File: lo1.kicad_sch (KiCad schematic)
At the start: 1 part

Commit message: lo1 schematic
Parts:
- added C1, C10, C11, C15, C2, C6: 100nF, ar_passives:C_0402, symbol #bt-db:capacitor/CAPC-00573
- added C12, C13, C14, C7: 1uF, ar_passives:C_0402, symbol #bt-db:capacitor/CAPC-00622
- added C16, C17, C18, C19: 22pF, ar_passives:C_0201, symbol #bt-db:capacitor/CAPC-00021
- added C3, C4, C8: 10uF, ar_passives:C_0402, symbol #bt-db:capacitor/CAPC-00667
- added C5: 470nF, ar_passives:C_0402, symbol #bt-db:capacitor/CAPC-00613
- added C9: 10nF, ar_passives:C_0402, symbol #bt-db:capacitor/CAPC-00514
- added CLF1: 0pF, ar_passives:C_0603, symbol #bt-db:capacitor/CAPC-00674
- added CLF2, CLF3: 0pF, ar_passives:C_0402, symbol #bt-db:capacitor/CAPC-00415
- added RLF2, RLF3: TBD, ar_passives:R_0402, symbol #bt-db:resistor/RESI-00693
- U3: footprint ar_discrete:QFN40 -> ar_ic:QFN40
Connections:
- net GND: now also C10.2, C11.2, C12.2, C13.2, C14.2, C15.2, C3.2, C4.2, C5.1, C6.2, C7.2, C8.2, C9.2, CLF1.2, CLF2.2, CLF3.1
- net SYN_CE: now reaches U3.1 (CE)
- net at U3.10 (VregIN): now also C7.1
- net LO1_3V3_SYN: now reaches U3.11 (VccCP)
- net LO1_3V3_SYN: now also U3.15 (VccMASH), U3.26 (VccVCO2), U3.37 (VccVCO), U3.7 (VccDIG), C10.1, C11.1, C12.1, C13.1, C14.1
- net at U3.12 (CPout): now also CLF1.1, RLF2.1, RLF3.2
- net SYN_SCK: now reaches U3.16 (SCK)
- net SYN_SDI: now reaches U3.17 (SDI)
- net at U3.18 (RFoutBM): now also C19.1
- net at U3.19 (RFoutBP): now also C18.1
- net SYN_MUX: now reaches U3.20 (MUXout)
- net LO1_3V3_BUF: now reaches U3.21 (VccBUF)
- net LO1_3V3_BUF: now also C15.1
- net at U3.22 (RFoutAM): now also C17.1
- net at U3.23 (RFoutAP): now also C16.1
- net SYN_~{CS}: now reaches U3.24 (~{CS})
- net at U3.27 (VbiasVCO2): now also C6.1
- net at U3.29 (VrefVCO2): now also C8.1
- net at U3.3 (VbiasVCO): now also C5.2
- net SYN_RC: now reaches U3.30 (RampClk)
- net SYN_RD: now reaches U3.32 (RampDir)
- net at U3.33 (VbiasVARAC): now also C4.1
- net at U3.35 (Vtune): now also CLF3.2, RLF3.1
- net at U3.36 (VrefVCO): now also C3.1
- net at U3.38 (VregVCO): now also C9.1
- net OSC_P: now reaches U3.8 (OSCinP)
- net OSC_P: now also C1.2
- net OSC_N: now reaches U3.9 (OSCinM)
- net OSC_N: now also C2.2
- new net: CLF2.1, RLF2.2
- new net REF_N: C2.1
- new net REF_P: C1.1
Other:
- note added: "11"
- note added: "15"
- note added: "26"
- note added: "37"
- note added: "7"

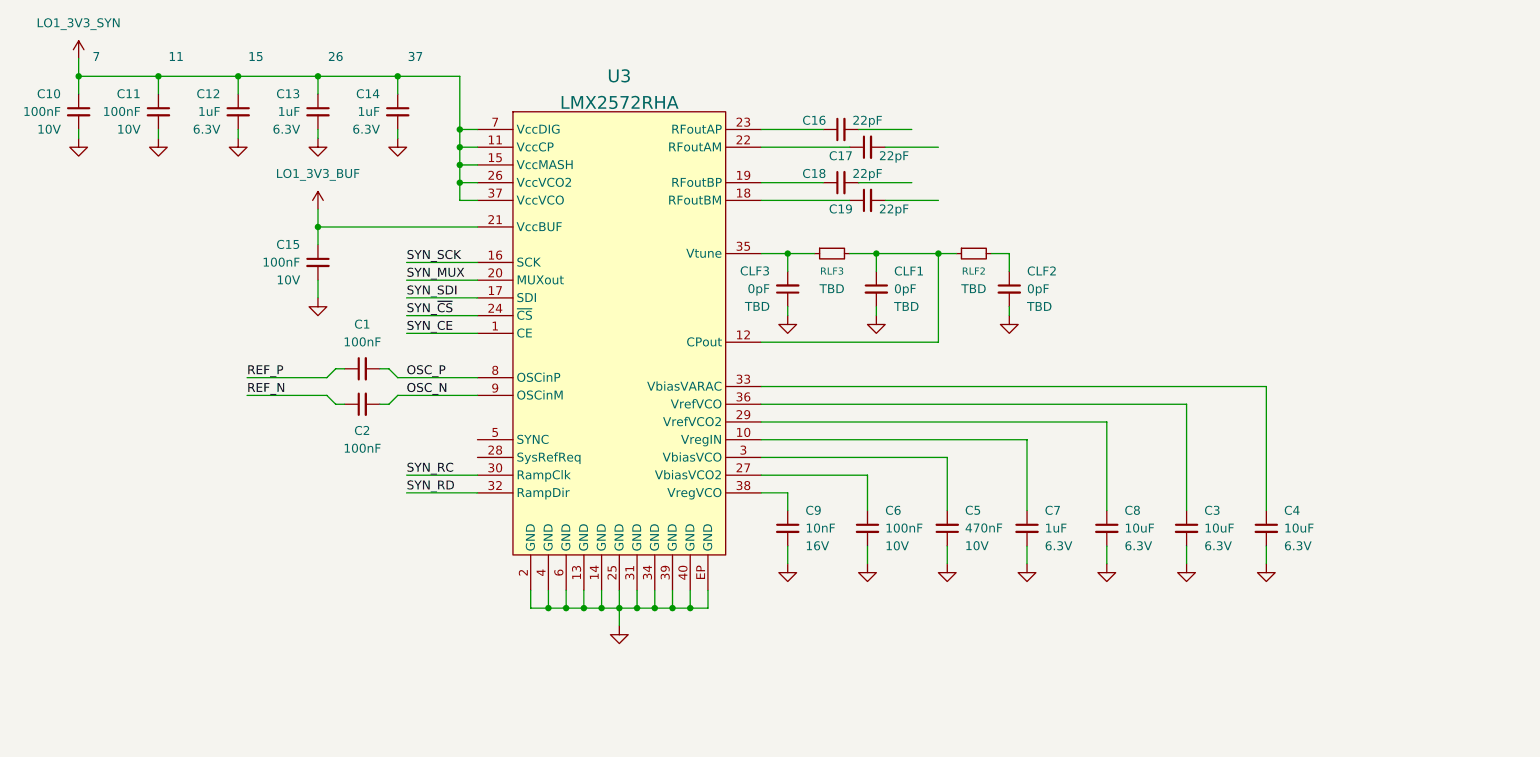
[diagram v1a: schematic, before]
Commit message: added labels to LO, duplicated to LO2
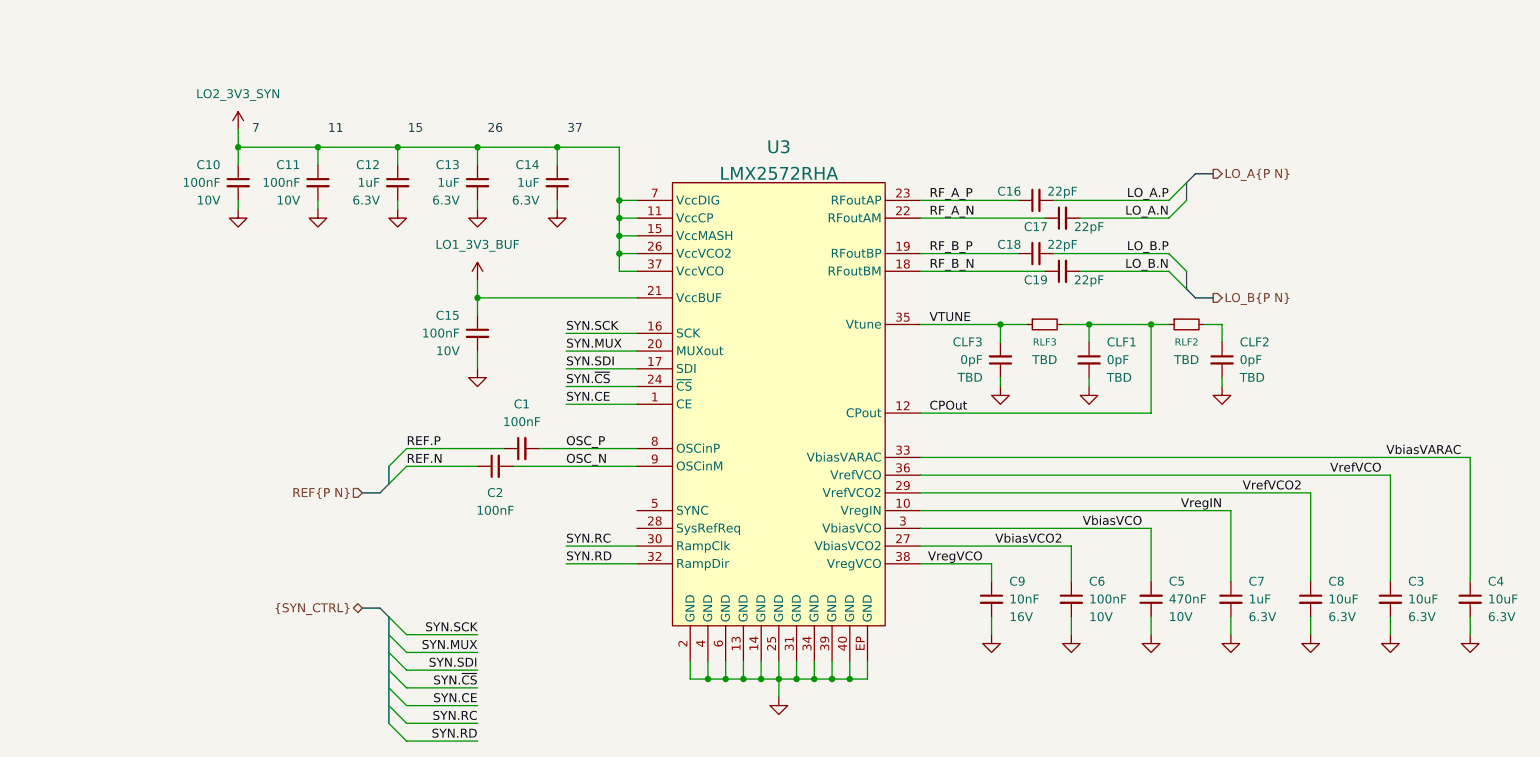
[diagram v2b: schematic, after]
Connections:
- net VrefVCO: now reaches C3.1, U3.36 (VrefVCO)
- net RF_A_N: now reaches C17.1, U3.22 (RFoutAM)
- net LO_A.N: now reaches C17.2
- net VregIN: now reaches C7.1, U3.10 (VregIN)
- net RF_A_P: now reaches C16.1, U3.23 (RFoutAP)
- net LO_A.P: now reaches C16.2
- net VbiasVCO2: now reaches C6.1, U3.27 (VbiasVCO2)
- net VrefVCO2: now reaches C8.1, U3.29 (VrefVCO2)
- net VTUNE: now reaches CLF3.2, RLF3.1, U3.35 (Vtune)
- net CPOut: now reaches CLF1.1, RLF2.1, RLF3.2, U3.12 (CPout)
- net RF_B_N: now reaches C19.1, U3.18 (RFoutBM)
- net LO_B.N: now reaches C19.2
- net RF_B_P: now reaches C18.1, U3.19 (RFoutBP)
- net VbiasVCO: now reaches C5.2, U3.3 (VbiasVCO)
- net VbiasVARAC: now reaches C4.1, U3.33 (VbiasVARAC)
- net VregVCO: now reaches C9.1, U3.38 (VregVCO)
- net LO_B.P: now reaches C18.2
- net LO1_3V3_SYN renamed LO2_3V3_SYN
- net REF_N renamed REF.N
- net REF_P renamed REF.P
- net SYN_CE renamed SYN.CE
- net SYN_MUX renamed SYN.MUX
- net SYN_RC renamed SYN.RC
- net SYN_RD renamed SYN.RD
- net SYN_SCK renamed SYN.SCK
- net SYN_SDI renamed SYN.SDI
- net SYN_~{CS} renamed SYN.~{CS}
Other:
- moved on the sheet: C1, C10, C11, C12, C13, C14, C15, C16, C17, C18, C19, C2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
